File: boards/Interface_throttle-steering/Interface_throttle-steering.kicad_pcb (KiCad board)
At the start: 2 copper layers, 70.6 x 48.8 mm, 59 parts, among them IC1 ATMEGA16M1, J1 micromatch_female_RA_20, J2 micromatch_female_RA_4, P1 CONN_02X03, Q1 SSM3K333R, Q2 SSM3K333R, Q3 SSM3K333R, U1 MCP6001RT, U2 CAN_Transceiver, U3 MCP6001RT, U4 TPS561201, Y1 Crystal_SMD

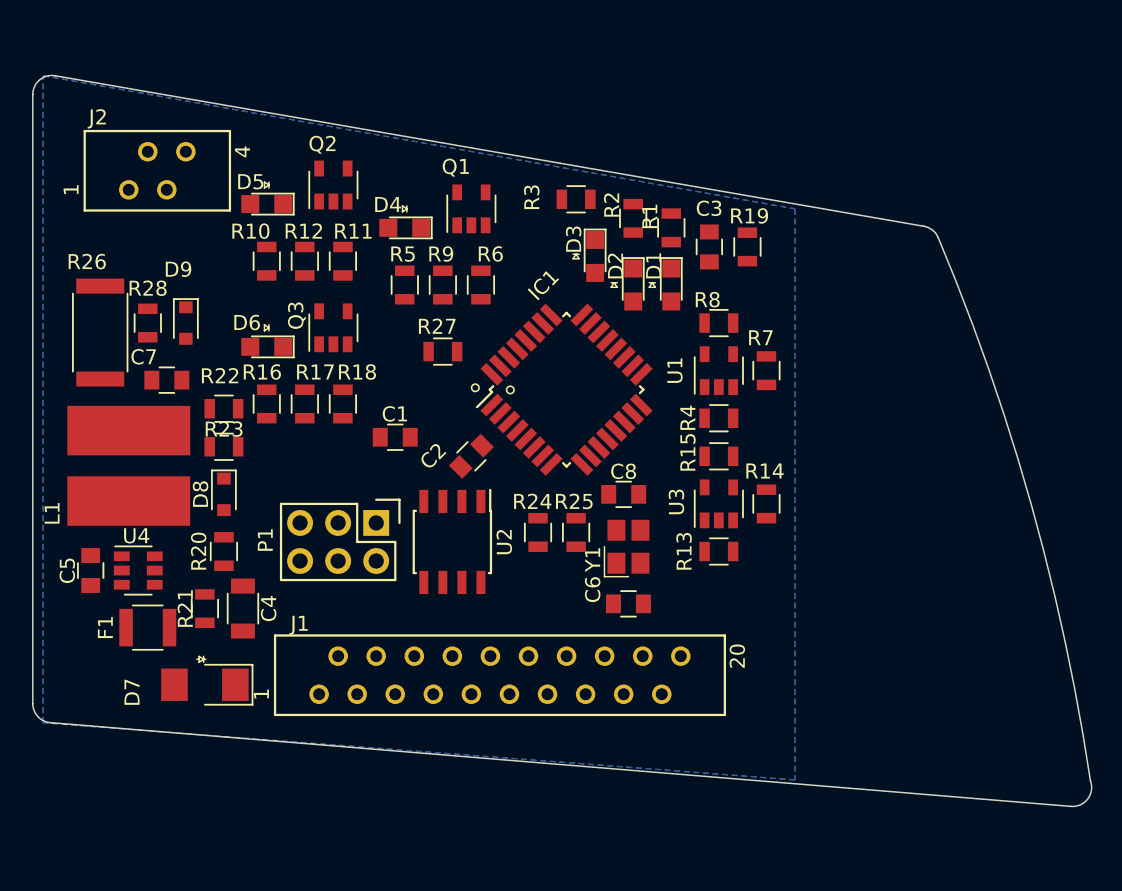
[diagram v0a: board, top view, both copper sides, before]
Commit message: Final throttle and interface design pending review
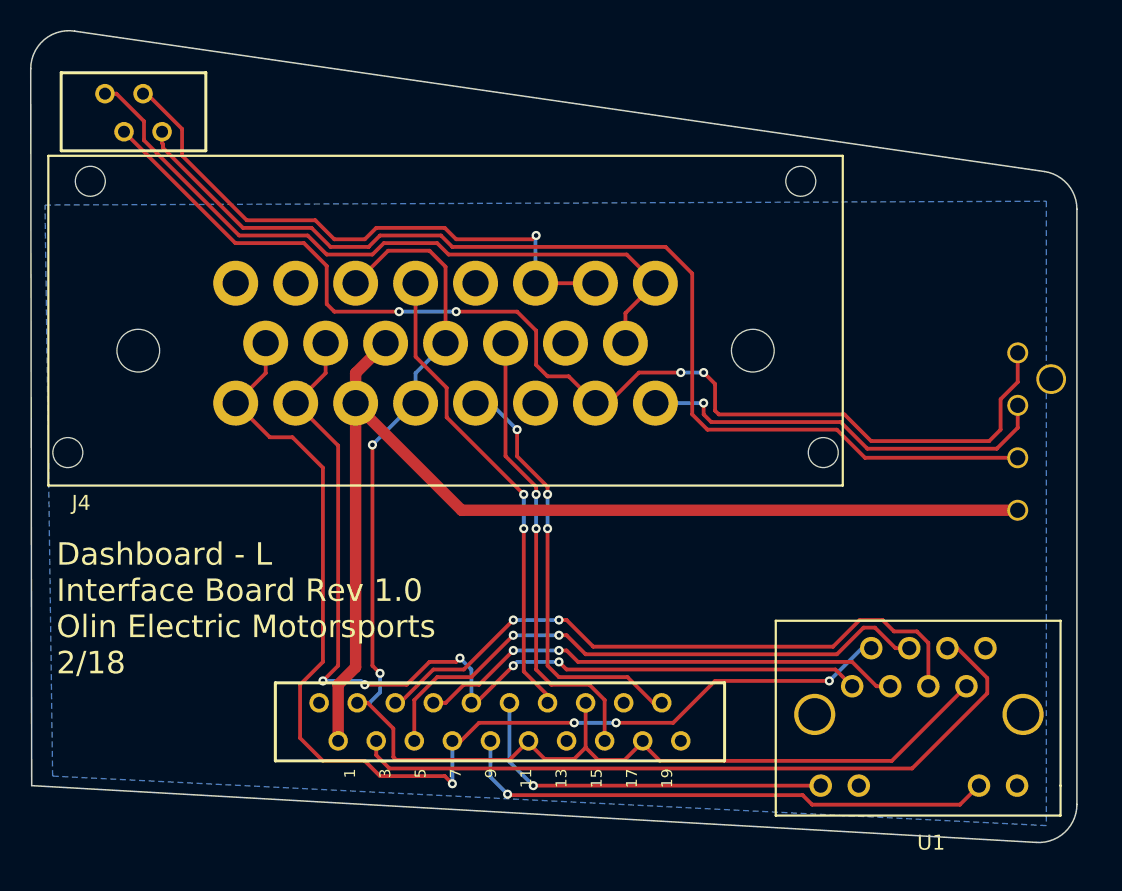
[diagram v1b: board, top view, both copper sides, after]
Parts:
- removed C1, C2, C5: C_0.1uF, footprints:C_0805_OEM
- removed C3: C_100pF, footprints:C_0805_OEM
- removed C4: C_22uF, footprints:C_1206_OEM
- removed C6, C8: C_30pF, footprints:C_0805_OEM
- removed C7: C_47uF, footprints:C_0805_OEM
- removed D1, D2, D3, D4, D5, D6: LED_0805, footprints:LED_0805_OEM
- removed D7: D_Zener_18V, footprints:DO-214AA
- removed D8, D9: LED_0805, footprints:D_0805_OEM
- removed F1: F_500mA_16V, footprints:Fuse_1210
- removed IC1: ATMEGA16M1, footprints:TQFP-32_7x7mm_Pitch0.8mm
- removed L1: L_4.7uH, footprints:4.7uH_Inductor_OEM
- removed P1: CONN_02X03, footprints:Pin_Header_Straight_2x03
- removed Q1, Q2, Q3: SSM3K333R, footprints:SOT-23-5_OEM
- removed R1, R2, R24, R25, R28, R3: R_200, footprints:R_0805_OEM
- removed R10, R15, R16, R20, R5, R7: R_1k, footprints:R_0805_OEM
- removed R11, R17, R6: R_100k, footprints:R_0805_OEM
- removed R12, R18, R21, R22, R27, R9: R_10k, footprints:R_0805_OEM
- removed R13, R4: R_1M, footprints:R_0805_OEM
- removed R14, R8: R_2.2k, footprints:R_0805_OEM
- removed R19: R_100, footprints:R_0805_OEM
- removed R23: R_55.1k, footprints:R_0805_OEM
- removed R26: R_0_Jumper, footprints:R_2512_OEM
- removed U2: CAN_Transceiver, footprints:SOIC-8_3.9x4.9mm_Pitch1.27mm_OEM
- removed U3: MCP6001RT, footprints:SOT-23-5_OEM
- removed U4: TPS561201, footprints:SOT-23-6_OEM
- removed Y1: Crystal_SMD, footprints:Crystal_SMD_FA238
- added J3: micromatch_male_20, footprints:micromatch_female_ra_20, B.Cu at (120.7, 88.8)
- added J4: Ampseal_23, footprints:Ampseal_23, F.Cu at (103.5, 65.3)
- J1: value micromatch_female_RA_20 -> micromatch_male_4; footprint footprints:micromatch_female_ra_20 -> footprints:micromatch_female_ra_4; moved to B.Cu
- J2: value micromatch_female_RA_4 -> Ultrafit_4; footprint footprints:micromatch_female_ra_4 -> footprints:Ultrafit_4; moved to B.Cu
- U1: value MCP6001RT -> RJ45; footprint footprints:SOT-23-5_OEM -> footprints:RJ45-Vertical
- moved J2 56.6 mm to (162.2, 70.7), turned to 0 degrees
- moved J1 42.5 mm to (106.4, 48.2), turned to 270 degrees
- moved U1 28.5 mm to (149.0, 94.4), turned to 0 degrees
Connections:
- J1 pad 1: GND -> /BOTS_sense
- J1 pad 2: +12V -> /BOTS_In/E-Stop_Out
- J1 pad 3: VCC -> /BSPD_In/Crash_Sensor_Out
- J1 pad 4: /MOSI -> /RTD_LS
- J2 pad 1: /SS_BOTS -> /BOTS_In/E-Stop_Out
- J2 pad 2: /SS_Cockpit_EStop -> /E-Stop_In/Connector_to_HVD_Out
- J2 pad 3: /SS_Inertia_Switch -> /RTD_LS
- J2 pad 4: Net-(J2-Pad4) -> /12V
- U1 pad 1: /Throttle2OutR -> /CAN_low
- U1 pad 2: VCC -> /CAN_high
- U1 pad 3: /Throttle_Right_Sense -> /RESET
- U1 pad 4: Net-(R7-Pad2) -> /SCK
- U1 pad 5: GND -> /MISO
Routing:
- net /5V: track 0.00 -> 91.2 mm, vias 0 -> 2
- net /BOTS_In/E-Stop_Out: track 0.00 -> 78.5 mm, vias 0 -> 4
- net /CAN_high: track 0.00 -> 75.9 mm, vias 0 -> 4
- net /12V: track 0.00 -> 75.0 mm
- net /RTD_LS: track 0.00 -> 72.8 mm
- net /CAN_low: track 0.00 -> 65.5 mm, vias 0 -> 5
- net /MOSI: track 0.00 -> 48.7 mm
- net /BOTS_sense: track 0.00 -> 48.2 mm
- net /MISO: track 0.00 -> 42.8 mm, vias 0 -> 2
- net /SCK: track 0.00 -> 39.4 mm, vias 0 -> 2
- net /BSPD_In/Crash_Sensor_Out: track 0.00 -> 39.2 mm, vias 0 -> 1
- net /LED1: track 0.00 -> 36.3 mm, vias 0 -> 1
- net /RESET: track 0.00 -> 32.9 mm, vias 0 -> 2
- net /Throttle_left: track 0.00 -> 31.6 mm, vias 0 -> 2
- net /Throttle_right: track 0.00 -> 30.8 mm, vias 0 -> 2
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- added copper zone on B.Cu, net /GND
- removed copper zone on B.Cu, net GND
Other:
- board size 70.6 x 48.8 mm -> 69.8 x 54.2 mm
- board text added: "1 3 5 7 9 11 13 15 17 19"
- board text added: "Dashboard - L Interface Board Rev 1.0 Olin Electric Motorsports 2/18"

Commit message: Rev 2 files for throttle-steering
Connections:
- J1 pad 1: /BOTS_sense -> /BOTS_In/E-Stop_Out
- J1 pad 2: /BOTS_In/E-Stop_Out -> /E-Stop_In/Connector_to_HVD_Out
- J1 pad 3: /BSPD_In/Crash_Sensor_Out -> /Crash_Sensor_In/BOTS_Out
- J4 pad 15: /BOTS_sense -> /Crash_Sensor_In/BOTS_Out
- J4 pad 8: /BOTS_sense -> /Crash_Sensor_In/BOTS_Out
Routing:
- net /Crash_Sensor_In/BOTS_Out: track 0.00 -> 48.4 mm, vias 0 -> 1
- net /BOTS_sense: track 48.2 -> 0.00 mm
- net /E-Stop_In/Connector_to_HVD_Out: track 28.0 -> 70.2 mm, vias 1 -> 2
- net /BSPD_In/Crash_Sensor_Out: track 39.2 -> 4.21 mm, vias 1 -> 0
- net /BOTS_In/E-Stop_Out: track 78.5 -> 79.9 mm

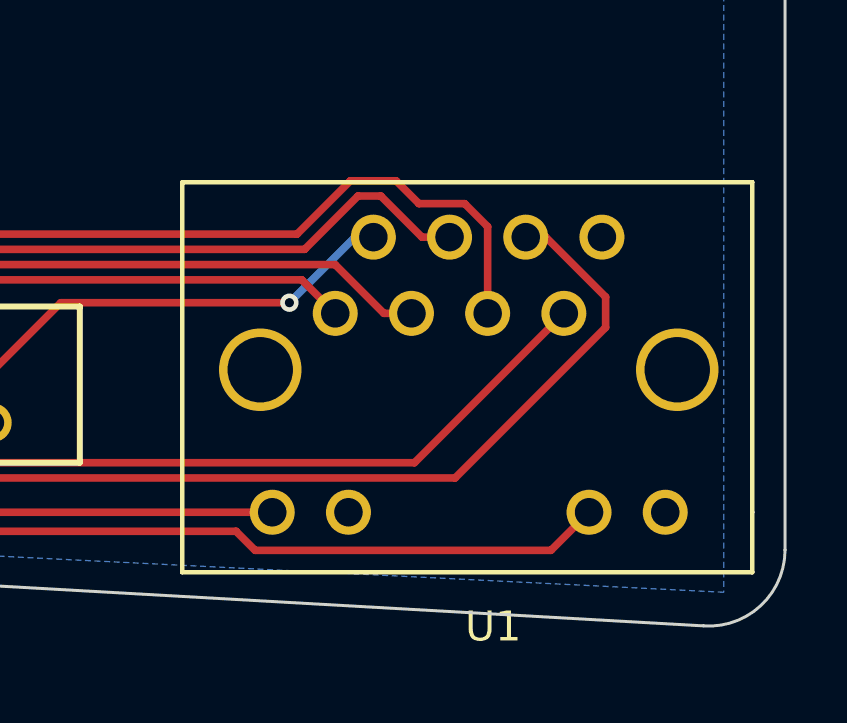
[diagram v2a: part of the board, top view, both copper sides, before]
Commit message: Started logger board, updated interface
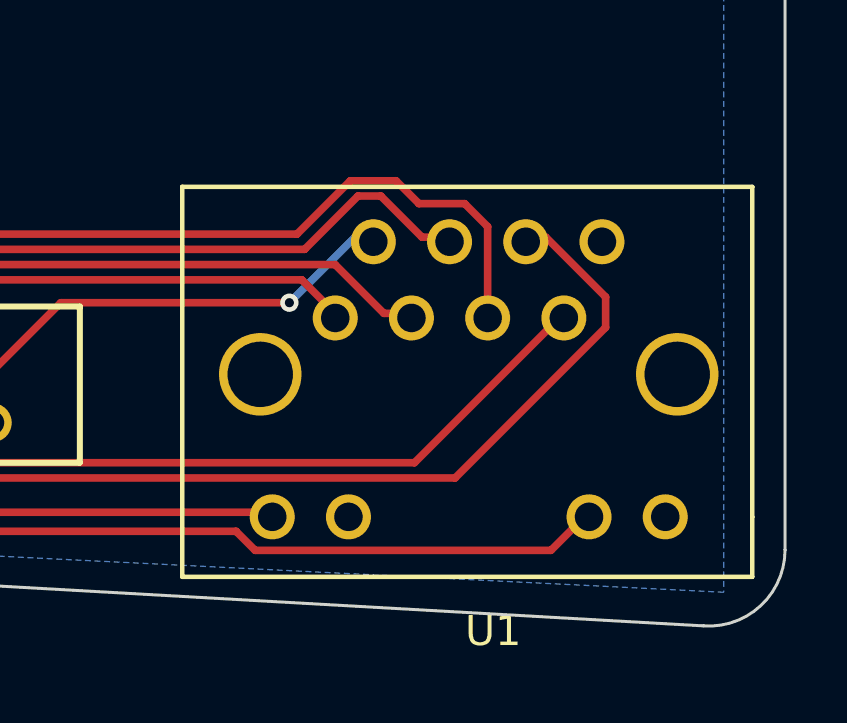
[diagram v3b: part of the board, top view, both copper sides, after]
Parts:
- moved U1 0.15 mm to (149.0, 94.5)
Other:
- board text added: "Corey Cochran-Lepiz"
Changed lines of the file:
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@@
     (links 46)
     (no_connects 0)
-    (area 96.279499 43.945246 167.7784 99.1984)
+    (area 96.279499 43.945246 166.177677 98.205014)
     (thickness 1.6)
-    (drawings 17)
+    (drawings 18)
     (tracks 286)
     (zones 0)
@@
     (pcbplotparams
       (layerselection 0x010f0_80000001)
-      (usegerberextensions true)
+      (usegerberextensions false)
       (excludeedgelayer true)
       (linewidth 0.100000)
@@
       (drillshape 0)
       (scaleselection 1)
-      (outputdirectory /home/corey/throttle-steering/))
+      (outputdirectory /home/corey/Music/))
   )
   (net 0 "")
@@
   )
   (module footprints:RJ45-Vertical (layer F.Cu)
-    (at 149.0345 94.361)
+    (at 149.0345 94.514)
     (fp_text reference U1 (at 7.366 3.81) (layer F.SilkS)
       (effects (font (size 1 1) (thickness 0.15)))
@@
       (rotate (xyz 0 0 0))
     )
+  )
+  (gr_text "Corey Cochran-Lepiz " (at 127 52.07) (layer B.SilkS)
+    (effects (font (size 1.5 1.5) (thickness 0.3)) (justify mirror))
   )
   (gr_text "Dashboard - L\nInterface Board Rev 1.0\nOlin Electric Motorsports\n2/18" (at 98.044 82.55) (layer F.SilkS)
@@
   (segment (start 105.156 51.562) (end 105.156 51.816) (width 0.254) (layer F.Cu) (net 7))
   (segment (start 105.0925 51.4985) (end 105.156 51.562) (width 0.254) (layer F.Cu) (net 7))
+  (segment (start 125.0745 75.989) (end 162.179 75.989) (width 0.762) (layer F.Cu) (net 9))
   (segment (start 118.005 68.8415) (end 118.005 68.9195) (width 0.762) (layer F.Cu) (net 9))
   (segment (start 118.005 68.9195) (end 125.0745 75.989) (width 0.762) (layer F.Cu) (net 9))
-  (segment (start 125.0745 75.989) (end 162.179 75.989) (width 0.762) (layer F.Cu) (net 9))
   (segment (start 118.005 68.8415) (end 118.005 66.8415) (width 0.762) (layer F.Cu) (net 9))
   (segment (start 118.005 66.8415) (end 120.005 64.8415) (width 0.762) (layer F.Cu) (net 9))

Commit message: Final dashboard L interface revision.
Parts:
- moved J2 0.89 mm to (163.1, 70.7), turned to 180 degrees
- moved U1 0.80 mm to (149.3, 95.3)
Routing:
- net /12V: track 75.0 -> 90.1 mm
- net /E-Stop_In/Connector_to_HVD_Out: track 70.2 -> 71.8 mm, vias 2 -> 1
- net /BOTS_In/E-Stop_Out: track 79.9 -> 78.5 mm, vias 4 -> 3
- net /CAN_low: track 65.5 -> 66.7 mm
- net /MISO: track 42.8 -> 43.9 mm
- net /RESET: track 32.9 -> 33.8 mm
- net /RTD_LS: track 72.8 -> 72.0 mm
- net /LED2: track 25.4 -> 26.0 mm
- net /SCK: track 39.4 -> 40.0 mm
- net /MOSI: track 48.7 -> 48.1 mm
- net /LED1: track 36.3 -> 36.9 mm
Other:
- board text added: "1"
- board text added: "15"
- board text added: "16"
- board text added: "23"
- board text added: "8"
- board text added: "9"
